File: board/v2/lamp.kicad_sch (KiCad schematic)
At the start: 42 parts, among them J1 Conn_01x01_Female, J2 Conn_01x01_Female, J3 Conn_01x01_Female, J4 Conn_01x01_Female, J5 Conn_01x01_Female, J6 Conn_01x01_Female, J7 Conn_01x01_Female, J8 Conn_ARM_JTAG_SWD_10, Q1 SIA483DJ-T1-GE3‎, U1 STM32G071GxU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

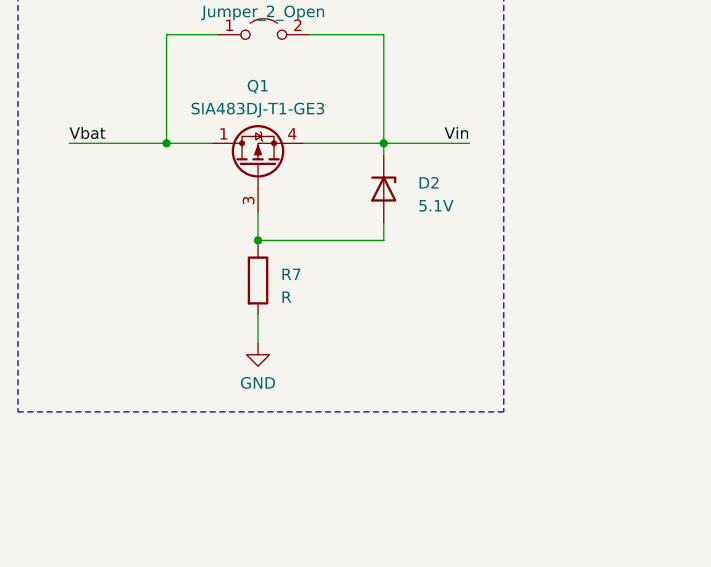
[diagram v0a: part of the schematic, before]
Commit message: hardware: Set R7 value
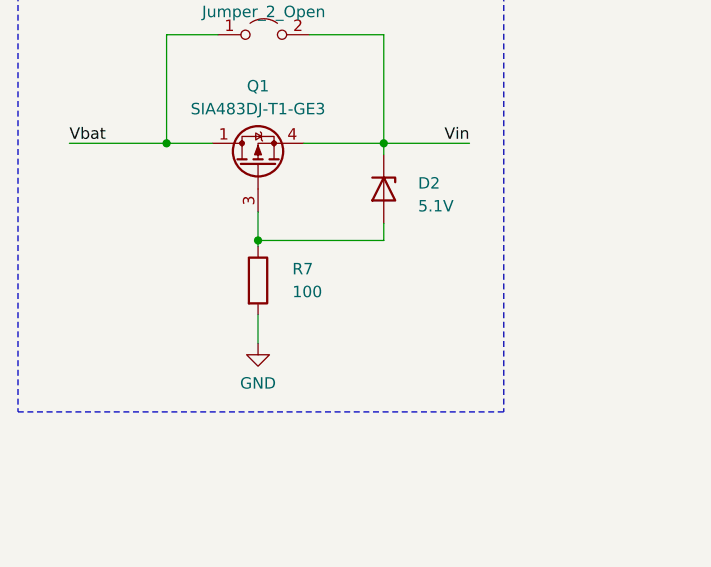
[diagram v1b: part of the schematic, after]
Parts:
- R7: value R -> 100
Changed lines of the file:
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@@
   (symbol (lib_name "Device:R_1") (lib_id "Device:R") (at -40.64 50.8 0) (unit 1)
     (in_bom yes) (on_board yes) (fields_autoplaced)
-    (property "Reference" "R7" (id 0) (at -38.1 50.1649 0)
+    (property "Reference" "R7" (id 0) (at -36.83 49.5299 0)
       (effects (font (size 1.27 1.27)) (justify left))
     )
-    (property "Value" "R" (id 1) (at -38.1 52.7049 0)
+    (property "Value" "100" (id 1) (at -36.83 52.0699 0)
       (effects (font (size 1.27 1.27)) (justify left))
     )

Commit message: hw: Changes
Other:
- note added: "G = 101 V/V f_co = 300 Hz"
- note added: "Overall r_m = 1.01 V/A"
- note removed: "G = 121 f_co = 300 Hz"
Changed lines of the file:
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@@
+    (effects (font (size 1.27 1.27)) (justify left bottom))
+  )
+  (text "Overall r_m = 1.01 V/A" (at 198.12 102.87 0)
     (effects (font (size 1.27 1.27)) (justify left bottom))
   )
@@
     (effects (font (size 1.27 1.27)) (justify left bottom))
   )
-  (text "G = 121\nf_co = 300 Hz" (at 256.54 114.3 0)
+  (text "G = 101 V/V\nf_co = 300 Hz" (at 256.54 114.3 0)
     (effects (font (size 1.27 1.27)) (justify left bottom))
   )

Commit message: board: Hardware fixes from assembly
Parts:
- D2: value 5.1V -> 15V
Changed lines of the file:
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@@
   (symbol (lib_id "Device:D_Zener") (at -26.67 40.64 270) (unit 1)
     (in_bom yes) (on_board yes) (fields_autoplaced)
-    (property "Reference" "D2" (id 0) (at -22.86 40.0049 90)
-      (effects (font (size 1.27 1.27)) (justify left))
-    )
-    (property "Value" "5.1V" (id 1) (at -22.86 42.5449 90)
+    (property "Reference" "D2" (id 0) (at -22.86 39.3699 90)
+      (effects (font (size 1.27 1.27)) (justify left))
+    )
+    (property "Value" "15V" (id 1) (at -22.86 41.9099 90)
       (effects (font (size 1.27 1.27)) (justify left))
     )
@@
     )
     (path "/8037ace0-5e49-4182-b38f-9fec37db3935"
-      (reference "D2") (unit 1) (value "5.1V") (footprint "Diode_SMD:D_SOD-123")
+      (reference "D2") (unit 1) (value "15V") (footprint "Diode_SMD:D_SOD-123")
     )
     (path "/00000000-0000-0000-0000-00005b3bf396"
@@
     )
     (path "/3810dab8-e421-47e2-9c2c-b9e82db49855"
-      (reference "R7") (unit 1) (value "R") (footprint "Resistor_SMD:R_0603_1608Metric")
+      (reference "R7") (unit 1) (value "100") (footprint "Resistor_SMD:R_0603_1608Metric")
     )
     (path "/00000000-0000-0000-0000-00005b38af5e"

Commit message: hw: Fix RESET line on JTAG connector
Previously this was disconnected due to a net name mismatch.
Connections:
- net RESET is gone; now on net ~{RESET}: U1.5 (~{RST}/PF2)
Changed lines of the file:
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@@
     (title "LED driver")
     (date "2021-07-30")
-    (rev "5")
+    (rev "${REVISION}")
     (company "Ben Gamari")
   )
@@
     (effects (font (size 1.27 1.27)) (justify left bottom))
   )
-  (label "RESET" (at 98.425 136.525 180)
+  (label "~{RESET}" (at 98.425 136.525 180)
     (effects (font (size 1.27 1.27)) (justify right bottom))
   )

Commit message: hw: Larger package for LDO input cap
0603 was too small for a realistic capacitance.
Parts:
- C4: footprint Capacitor_SMD:C_0603_1608Metric -> Capacitor_SMD:C_0805_2012Metric_Pad1.18x1.45mm_HandSolder
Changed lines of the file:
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@@
       (effects (font (size 1.27 1.27)) (justify left))
     )
-    (property "Footprint" "Capacitor_SMD:C_0603_1608Metric" (id 2) (at 113.3602 182.245 0)
+    (property "Footprint" "Capacitor_SMD:C_0805_2012Metric_Pad1.18x1.45mm_HandSolder" (id 2) (at 113.3602 182.245 0)
       (effects (font (size 1.27 1.27)) hide)
     )
@@
     )
     (path "/00000000-0000-0000-0000-00005b41eebb"
-      (reference "C4") (unit 1) (value "4.7u") (footprint "Capacitor_SMD:C_0603_1608Metric")
+      (reference "C4") (unit 1) (value "4.7u") (footprint "Capacitor_SMD:C_0805_2012Metric_Pad1.18x1.45mm_HandSolder")
     )
     (path "/00000000-0000-0000-0000-00005b3b4dac"
